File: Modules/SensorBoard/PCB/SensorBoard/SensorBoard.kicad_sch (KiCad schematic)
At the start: 1 part

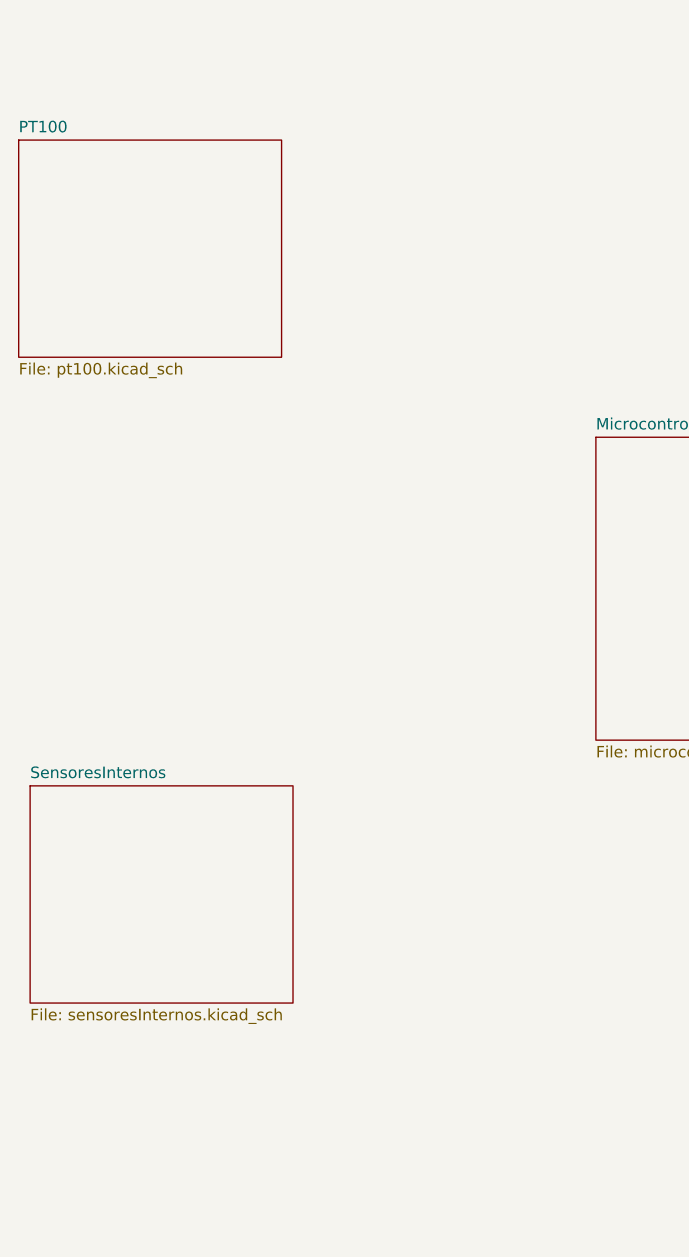
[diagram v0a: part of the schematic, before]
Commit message: sensor board basic components
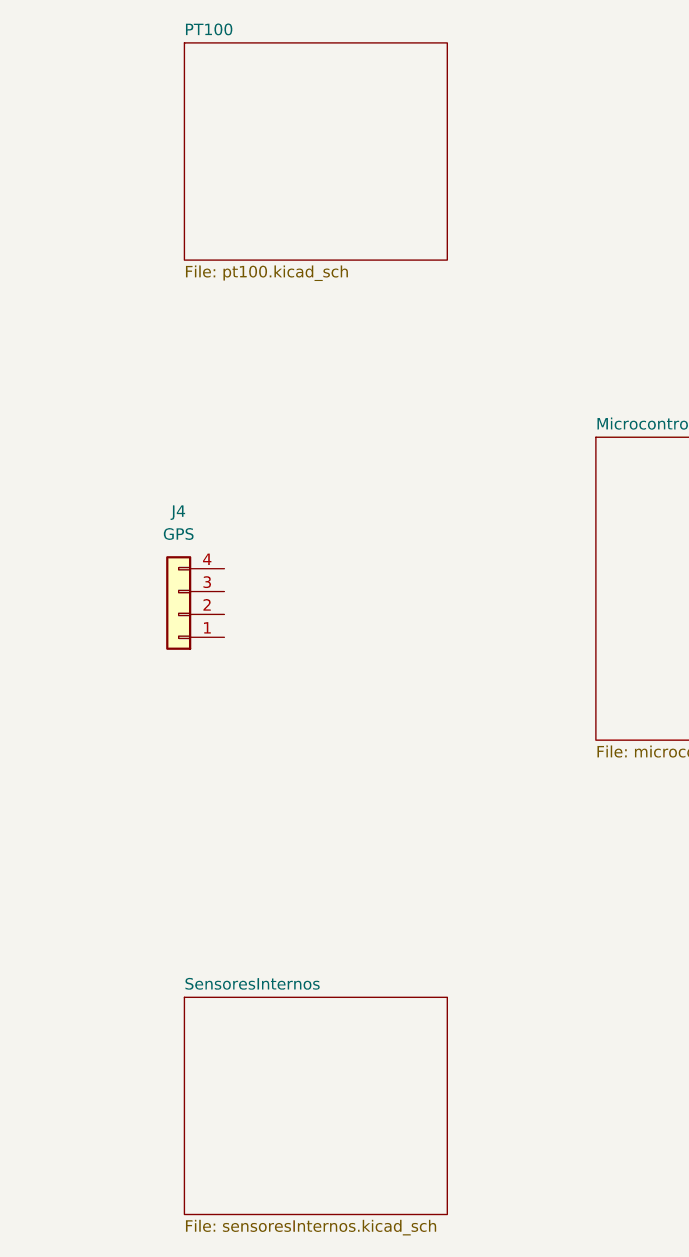
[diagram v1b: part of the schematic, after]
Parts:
- added J4: GPS, Connector_JST:JST_PH_S4B-PH-K_1x04_P2.00mm_Horizontal, symbol Connector_Generic:Conn_01x04
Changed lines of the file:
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@@
 (kicad_sch
-	(version 20231120)
+	(version 20250114)
 	(generator "eeschema")
-	(generator_version "8.0")
+	(generator_version "9.0")
 	(paper "A4")
 	(no_connect
@@
 	)
 	(symbol
+		(lib_id "Connector_Generic:Conn_01x04")
+		(at 67.31 86.36 180)
+		(unit 1)
+		(exclude_from_sim no)
+		(in_bom yes)
+		(on_board yes)
+		(dnp no)
+		(fields_autoplaced yes)
+		(property "Reference" "J4"
+			(at 67.31 74.93 0)
+			(effects
+				(font
+					(size 1.27 1.27)
+				)
+			)
+		)
+		(property "Value" "GPS"
+			(at 67.31 77.47 0)
+			(effects
+				(font
+					(size 1.27 1.27)
+				)
+			)
+		)
+		(property "Footprint" "Connector_JST:JST_PH_S4B-PH-K_1x04_P2.00mm_Horizontal"
+			(at 67.31 86.36 0)
+			(effects
+				(font
+					(size 1.27 1.27)
+				)
+				(hide yes)
+			)
+		)
+		(property "Datasheet" "~"
+			(at 67.31 86.36 0)
+			(effects
+				(font
+					(size 1.27 1.27)
+				)
+				(hide yes)
+			)
+		)
+		(property "Description" "Generic connector, single row, 01x04, script generated (kicad-library-utils/schlib/autogen/connector/)"
+			(at 67.31 86.36 0)
+			(effects
+				(font
+					(size 1.27 1.27)
+				)
+				(hide yes)
+			)
+		)
+		(pin "2"
+		)
+		(pin "4"
+		)
+		(pin "1"
+		)
+		(pin "3"
+		)
+		(instances
+			(project ""
+				(path "/fa219048-dcb4-48ee-a6b6-8b1fad43a054"
+					(reference "J4")
+					(unit 1)
+				)
+			)
+		)
+	)
+	(symbol
 		(lib_id "IcaroLib:Conector_General_Tarjetas")
 		(at 227.33 78.74 0)
@@
 	)
 	(sheet
-		(at 49.53 33.655)
+		(at 67.945 22.86)
 		(size 29.21 24.13)
+		(exclude_from_sim no)
+		(in_bom yes)
+		(on_board yes)
+		(dnp no)
 		(fields_autoplaced yes)
 		(stroke
@@
 		)
 		(property "Sheetname" "PT100"
-			(at 49.53 32.9434 0)
+			(at 67.945 22.1484 0)
 			(effects
 				(font
@@
 		)
 		(property "Sheetfile" "pt100.kicad_sch"
-			(at 49.53 58.3696 0)
+			(at 67.945 47.5746 0)
 			(effects
 				(font
@@
 		(at 113.665 66.675)
 		(size 38.1 33.655)
+		(exclude_from_sim no)
+		(in_bom yes)
+		(on_board yes)
+		(dnp no)
 		(fields_autoplaced yes)
 		(stroke
@@
 	)
 	(sheet
-		(at 50.8 105.41)
+		(at 67.945 128.905)
 		(size 29.21 24.13)
+		(exclude_from_sim no)
+		(in_bom yes)
+		(on_board yes)
+		(dnp no)
 		(fields_autoplaced yes)
 		(stroke
@@
 		)
 		(property "Sheetname" "SensoresInternos"
-			(at 50.8 104.6984 0)
+			(at 67.945 128.1934 0)
 			(effects
 				(font
@@
 		)
 		(property "Sheetfile" "sensoresInternos.kicad_sch"
-			(at 50.8 130.1246 0)
+			(at 67.945 153.6196 0)
 			(effects
 				(font
@@
 		)
 	)
+	(embedded_fonts no)
 )

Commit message: Finished Supply board
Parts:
- J4: footprint Connector_JST:JST_PH_S4B-PH-K_1x04_P2.00mm_Horizontal -> Connector_JST:JST_ZH_S6B-ZR-SM4A-TF_1x06-1MP_P1.50mm_Horizontal
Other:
- sheet Microcontroller ports: added I2C_BME{SDA SCL}, SPI_IMU{MOSI MISO SCK CS0}; removed none
- sheet SensoresInternos ports: added I2C_BME{SDA SCL}, SPI_IMU{MOSI MISO SCK CS0}; removed none
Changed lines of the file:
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@@
 		(at 214.63 66.04)
 	)
+	(bus
+		(pts
+			(xy 105.41 135.89) (xy 105.41 78.74)
+		)
+		(stroke
+			(width 0)
+			(type default)
+		)
+	)
+	(bus
+		(pts
+			(xy 97.79 135.89) (xy 105.41 135.89)
+		)
+		(stroke
+			(width 0)
+			(type default)
+		)
+	)
 	(wire
 		(pts
@@
 		)
 	)
+	(bus
+		(pts
+			(xy 109.22 88.9) (xy 114.3 88.9)
+		)
+		(stroke
+			(width 0)
+			(type default)
+		)
+	)
 	(wire
 		(pts
@@
 		)
 	)
+	(bus
+		(pts
+			(xy 97.79 142.24) (xy 109.22 142.24)
+		)
+		(stroke
+			(width 0)
+			(type default)
+		)
+	)
 	(wire
 		(pts
@@
 		(pts
 			(xy 210.82 71.12) (xy 214.63 71.12)
+		)
+		(stroke
+			(width 0)
+			(type default)
+		)
+	)
+	(bus
+		(pts
+			(xy 109.22 142.24) (xy 109.22 88.9)
+		)
+		(stroke
+			(width 0)
+			(type default)
+		)
+	)
+	(bus
+		(pts
+			(xy 105.41 78.74) (xy 114.3 78.74)
 		)
 		(stroke
@@
 			)
 		)
-		(property "Footprint" "Connector_JST:JST_PH_S4B-PH-K_1x04_P2.00mm_Horizontal"
+		(property "Footprint" "Connector_JST:JST_ZH_S6B-ZR-SM4A-TF_1x06-1MP_P1.50mm_Horizontal"
 			(at 67.31 86.36 0)
 			(effects
@@
 	)
 	(sheet
-		(at 67.945 22.86)
+		(at 68.58 22.86)
 		(size 29.21 24.13)
 		(exclude_from_sim no)
@@
 		)
 		(property "Sheetname" "PT100"
-			(at 67.945 22.1484 0)
+			(at 68.58 22.1484 0)
 			(effects
 				(font
@@
 		)
 		(property "Sheetfile" "pt100.kicad_sch"
-			(at 67.945 47.5746 0)
+			(at 68.58 47.5746 0)
 			(effects
 				(font
@@
 	)
 	(sheet
-		(at 113.665 66.675)
-		(size 38.1 33.655)
+		(at 114.3 67.31)
+		(size 38.1 33.02)
 		(exclude_from_sim no)
 		(in_bom yes)
@@
 		)
 		(property "Sheetname" "Microcontroller"
-			(at 113.665 65.9634 0)
+			(at 114.3 66.5984 0)
 			(effects
 				(font
@@
 		)
 		(property "Sheetfile" "microcontroller.kicad_sch"
-			(at 113.665 100.9146 0)
+			(at 114.3 101.5496 0)
 			(effects
 				(font
@@
 			)
 		)
+		(pin "I2C_BME{SDA SCL}" input
+			(at 114.3 78.74 180)
+			(effects
+				(font
+					(size 1.27 1.27)
+				)
+				(justify left)
+			)
+		)
+		(pin "SPI_IMU{MOSI MISO SCK CS0}" bidirectional
+			(at 114.3 88.9 180)
+			(effects
+				(font
+					(size 1.27 1.27)
+				)
+				(justify left)
+			)
+		)
 		(instances
 			(project "SensorBoard"
@@
 	)
 	(sheet
-		(at 67.945 128.905)
-		(size 29.21 24.13)
+		(at 57.15 129.54)
+		(size 40.64 17.78)
 		(exclude_from_sim no)
 		(in_bom yes)
@@
 		)
 		(property "Sheetname" "SensoresInternos"
-			(at 67.945 128.1934 0)
+			(at 57.15 128.8284 0)
 			(effects
 				(font
@@
 		)
 		(property "Sheetfile" "sensoresInternos.kicad_sch"
-			(at 67.945 153.6196 0)
+			(at 57.15 147.9046 0)
 			(effects
 				(font
@@
 			)
 		)
+		(pin "I2C_BME{SDA SCL}" input
+			(at 97.79 135.89 0)
+			(effects
+				(font
+					(size 1.27 1.27)
+				)
+				(justify right)
+			)
+		)
+		(pin "SPI_IMU{MOSI MISO SCK CS0}" bidirectional
+			(at 97.79 142.24 0)
+			(effects
+				(font
+					(size 1.27 1.27)
+				)
+				(justify right)
+			)
+		)

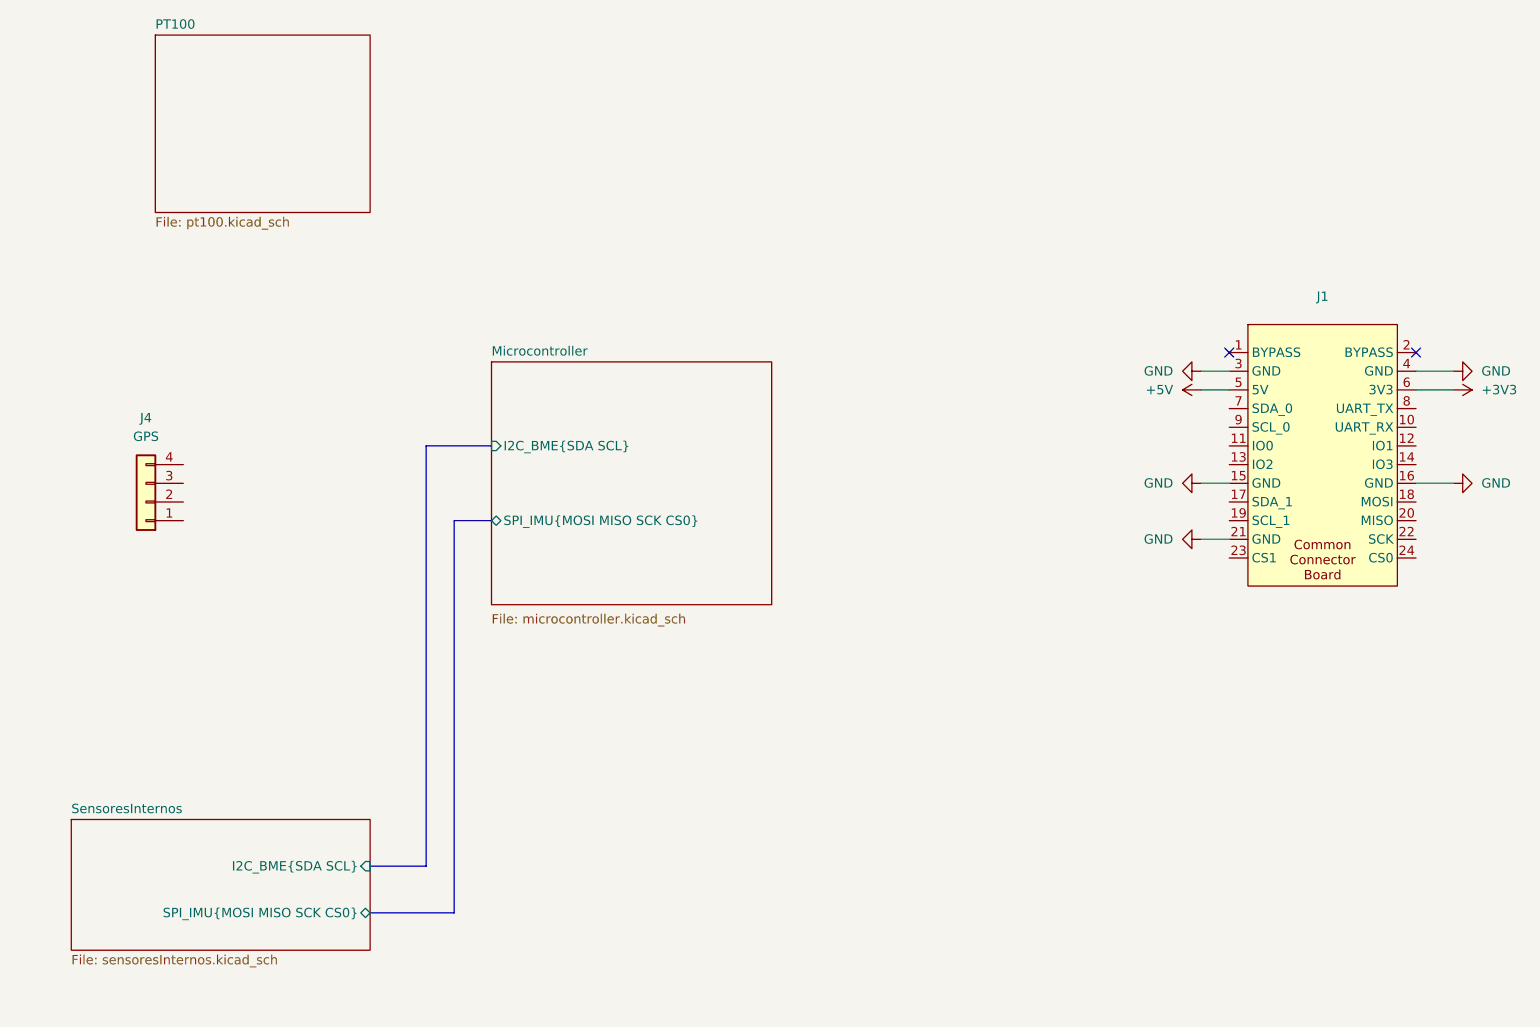
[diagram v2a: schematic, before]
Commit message: Enrutado de diseño de PT100 en la sensorboard
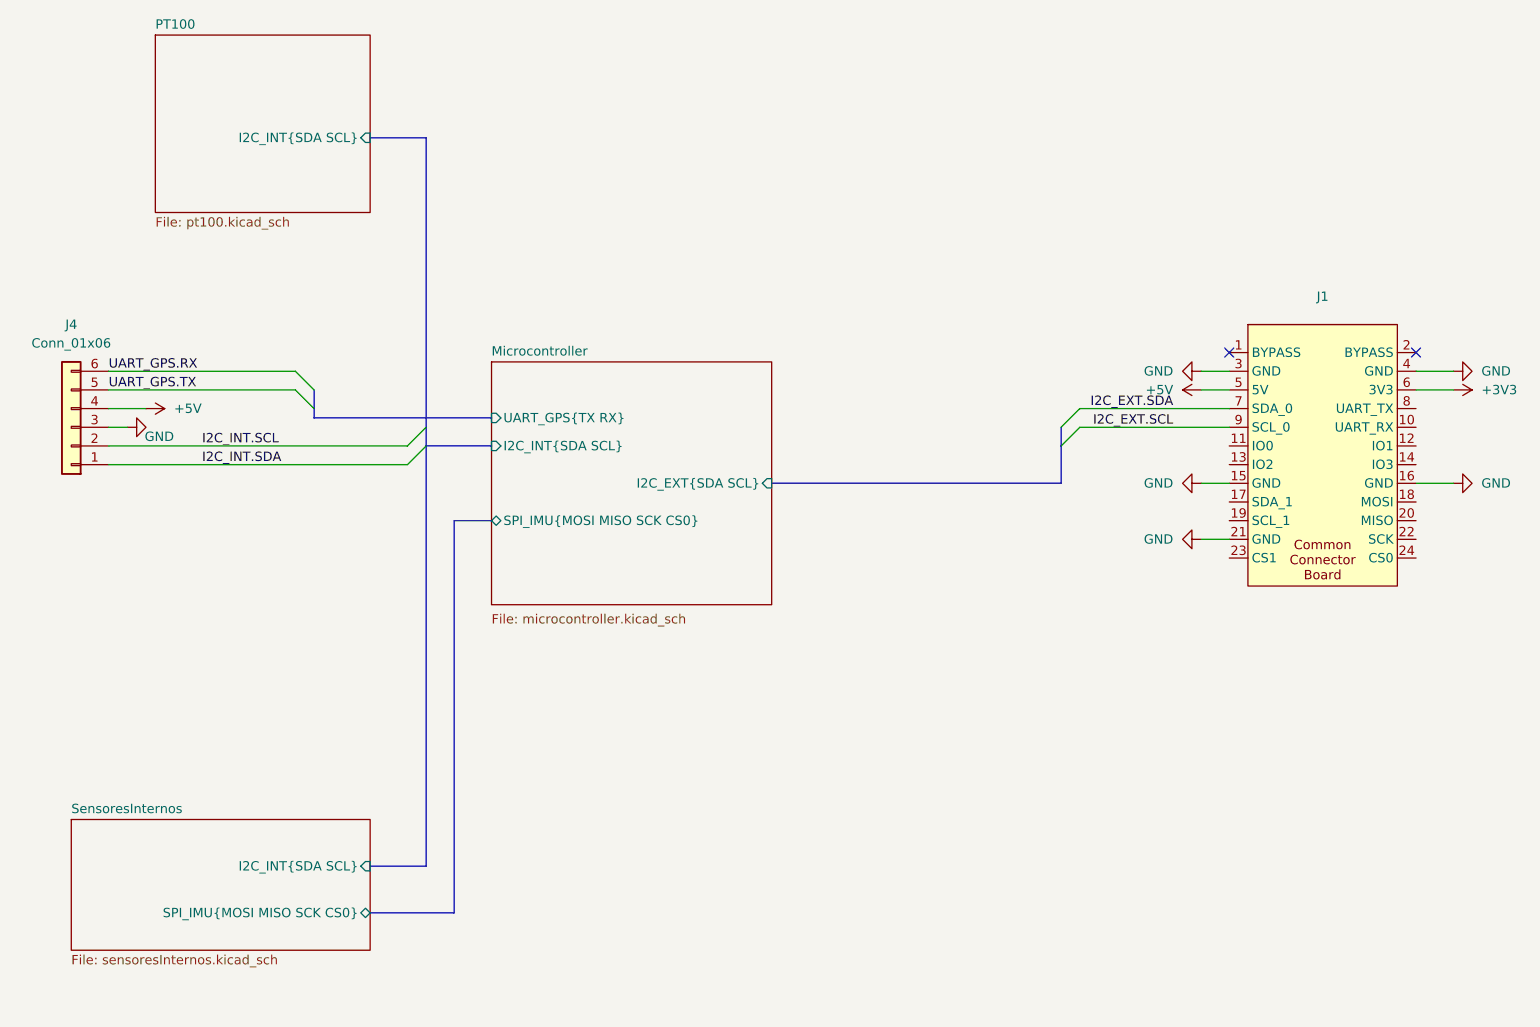
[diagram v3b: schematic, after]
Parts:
- removed J4: GPS, Connector_JST:JST_ZH_S6B-ZR-SM4A-TF_1x06-1MP_P1.50mm_Horizontal, symbol Connector_Generic:Conn_01x04
- added J4: Conn_01x06, Connector_JST:JST_ZH_S6B-ZR-SM4A-TF_1x06-1MP_P1.50mm_Horizontal, symbol Connector_Generic:Conn_01x06
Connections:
- net +5V: now also J4.4 (Pin_4)
- net GND: now also J4.3 (Pin_3)
- net I2C_EXT.SDA: now reaches J1.7 (SDA_0)
- net I2C_EXT.SCL: now reaches J1.9 (SCL_0)
- new net I2C_INT.SCL: J4.2 (Pin_2)
- new net I2C_INT.SDA: J4.1 (Pin_1)
- new net UART_GPS.RX: J4.6 (Pin_6)
- new net UART_GPS.TX: J4.5 (Pin_5)
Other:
- sheet Microcontroller ports: added I2C_EXT{SDA SCL}, I2C_INT{SDA SCL}, UART_GPS{TX RX}; removed I2C_BME{SDA SCL}
- sheet PT100 ports: added I2C_INT{SDA SCL}; removed none
- sheet SensoresInternos ports: added I2C_INT{SDA SCL}; removed I2C_BME{SDA SCL}

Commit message: Finished Sensor and Backplane boards
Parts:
- added R13, R14: 10k, Resistor_SMD:R_0603_1608Metric_Pad0.98x0.95mm_HandSolder, symbol Device:R
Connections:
- net +3V3: now also R13.2, R14.2
- net I2C_EXT.SCL: now also R14.1
- net I2C_EXT.SDA: now also R13.1
